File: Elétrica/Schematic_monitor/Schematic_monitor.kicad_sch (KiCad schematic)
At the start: 53 parts, among them J1 Conn_01x04, J2 USB_B_Micro, J3 Eletrode 1, J4 Eletrode 2, SW1 SW_Push, SW2 SW_SPDT, SW3 SW_SPDT, SW4 SW_SPDT, SW5 SW_SPDT, SW6 SW_SPDT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

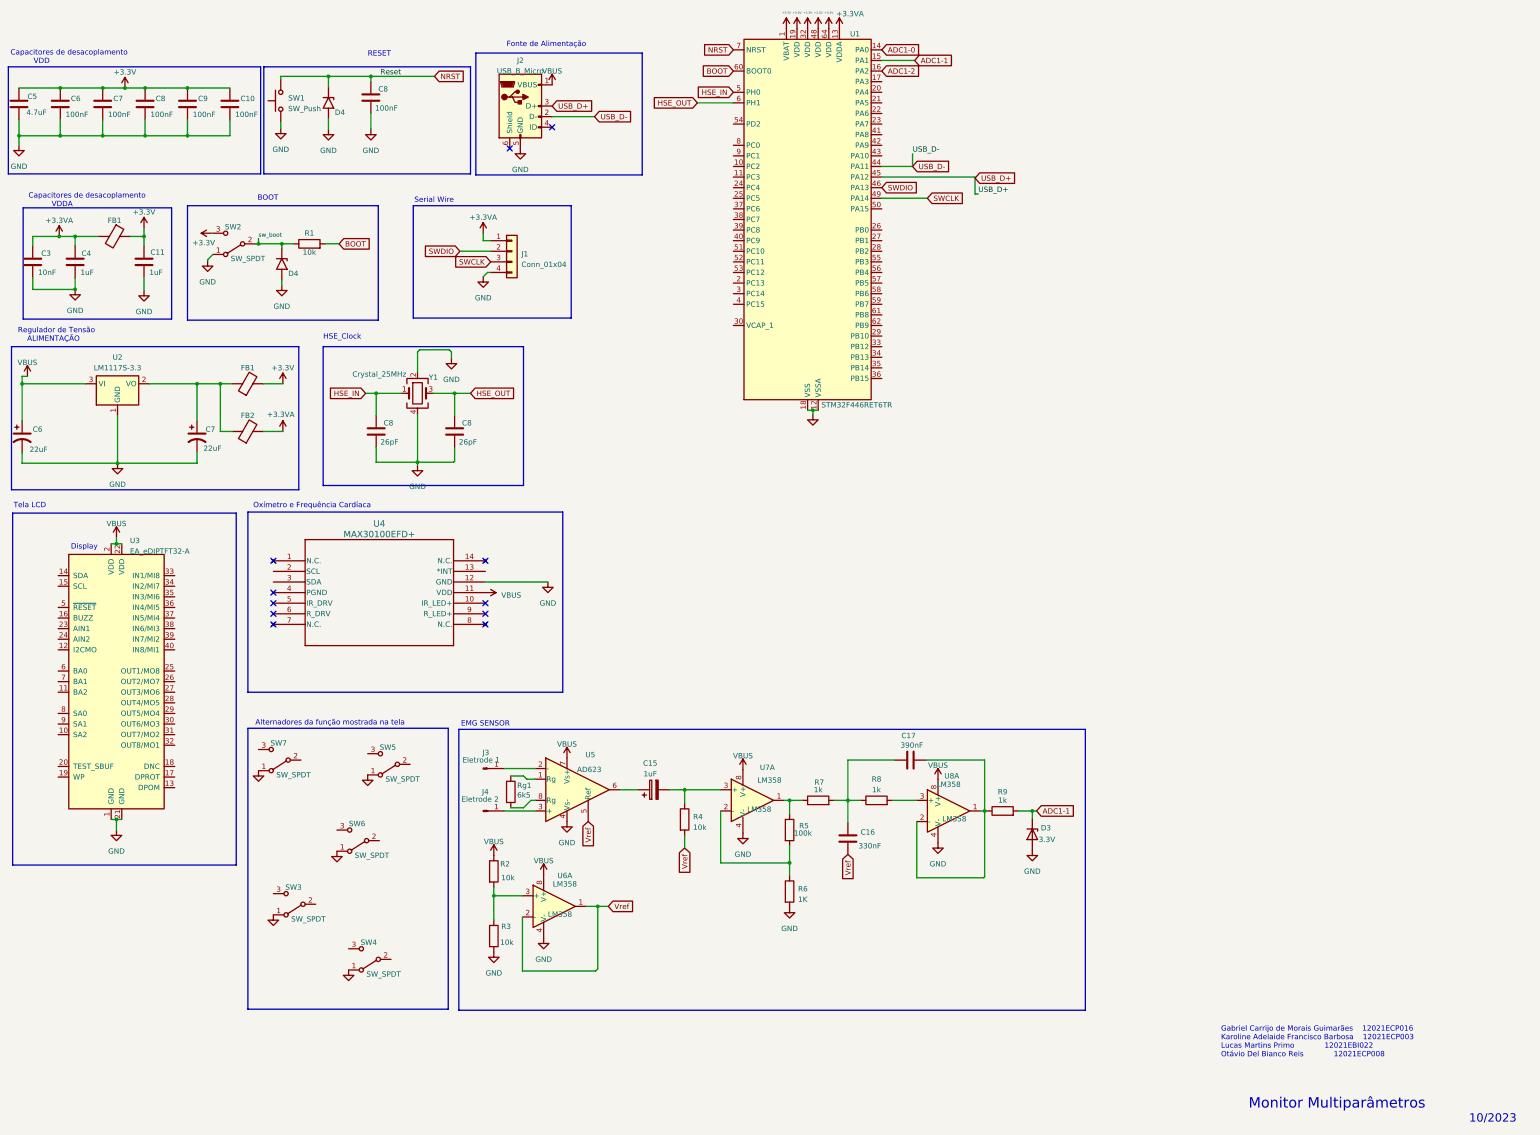
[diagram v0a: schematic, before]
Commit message: Correção Geral das pastas
Concertei diretório das pastas
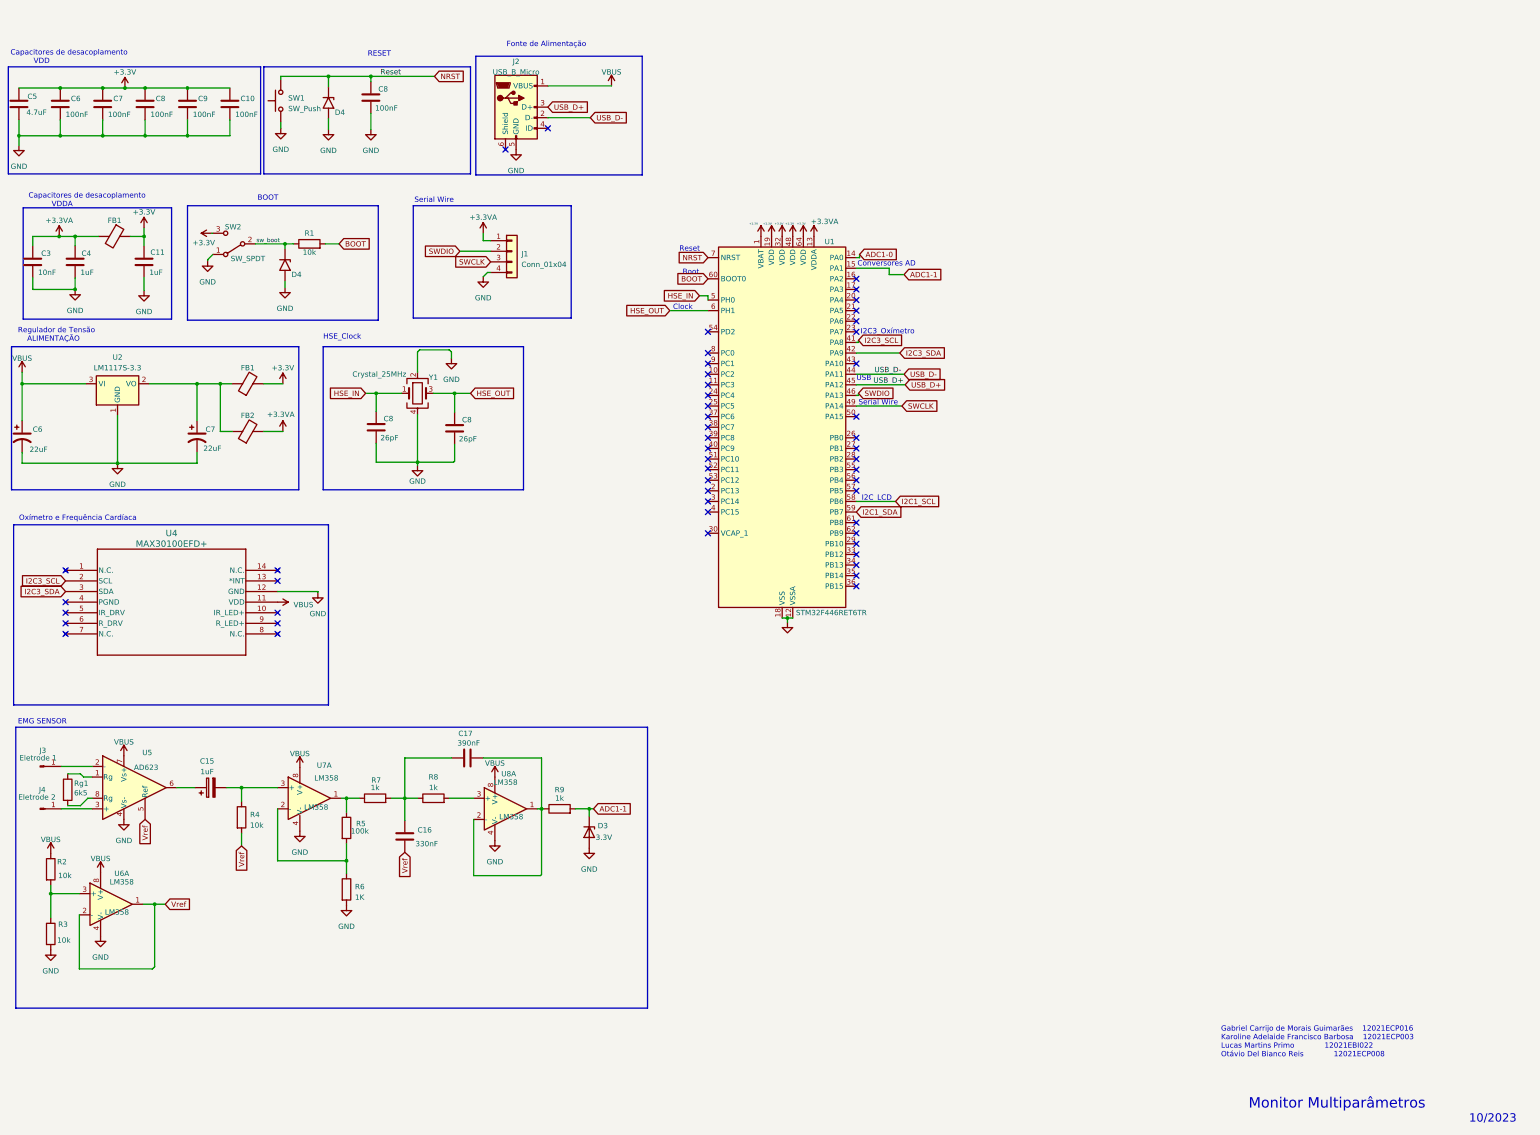
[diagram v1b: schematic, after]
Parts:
- removed SW3, SW4, SW5, SW6, SW7: SW_SPDT, Button_Switch_SMD:SW_DIP_SPSTx01_Slide_9.78x4.72mm_W8.61mm_P2.54mm, symbol Switch:SW_SPDT
- removed U3: EA_eDIPTFT32-A, Display:EA_eDIPTFT32-XXX, symbol Display_Graphic:EA_eDIPTFT32-A
- FB1: value FerriteBead -> New_Library:FerriteBead; footprint Inductor_SMD:L_0603_1608Metric -> Inductor_SMD:L_0603_1608Metric_Pad1.05x0.95mm_HandSolder
- FB2: footprint Inductor_SMD:L_0603_1608Metric -> Inductor_SMD:L_0603_1608Metric_Pad1.05x0.95mm_HandSolder
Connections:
- net I2C3_SCL: now reaches U4.2 (SCL)
- net I2C3_SCL: now also U1.41 (PA8)
- net I2C3_SDA: now reaches U4.3 (SDA)
- net I2C3_SDA: now also U1.42 (PA9)
- net I2C1_SCL: now reaches U1.58 (PB6)
- net I2C1_SDA: now reaches U1.59 (PB7)
- net ADC1-2: no longer names the net of U1.16 (PA2)
- no-connect marks 11 -> 51
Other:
- note added: "Boot"
- note added: "Clock"
- note added: "Conversores AD"
- note added: "I2C3_Oxímetro"
- note added: "I2C_LCD"
- note added: "Reset"
- note added: "USB"
- note removed: "Alternadores da função mostrada na tela"
- note removed: "Display"
- note removed: "Tela LCD"
- moved on the sheet: C15, C16, C17, C8, D3, D4, J2, J3, J4, R2, R3, R4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

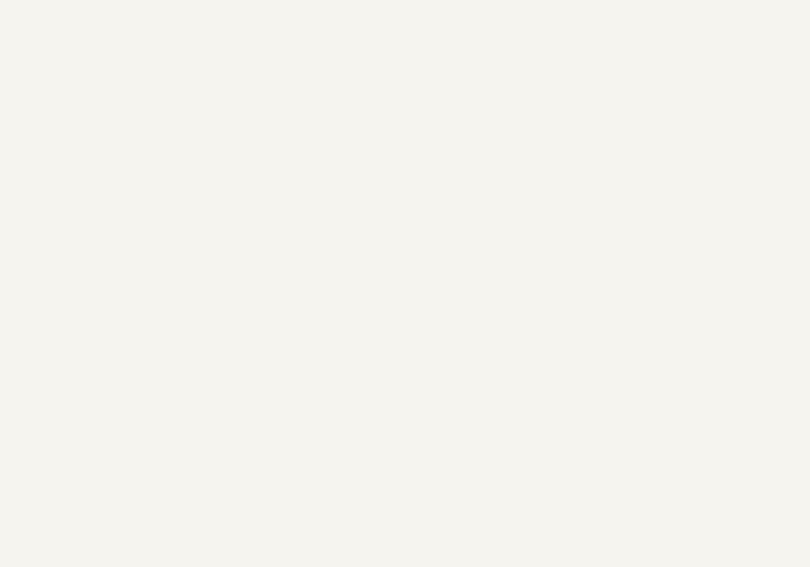
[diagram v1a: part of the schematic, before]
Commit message: Temp sensor
Adicionado sensor de temperatura
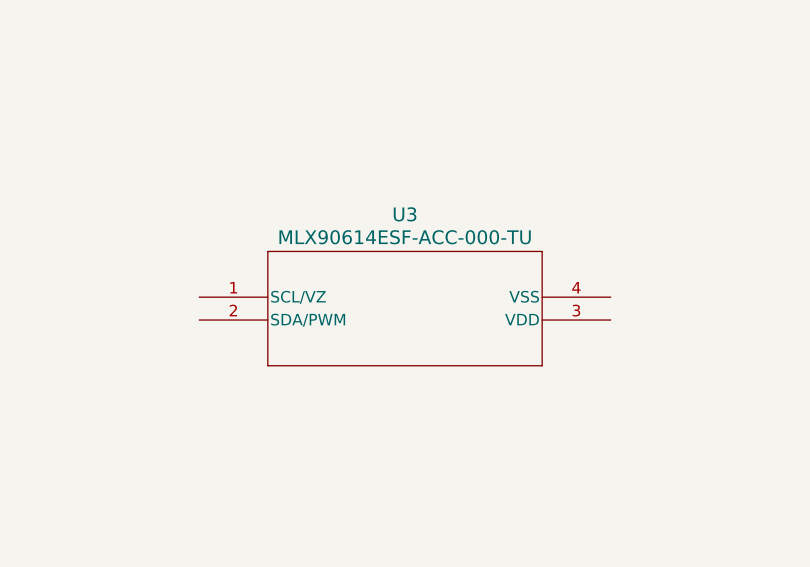
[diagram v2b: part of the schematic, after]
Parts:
- added U3: MLX90614ESF-ACC-000-TU, MLX90614xCC_MEL, symbol Temp_sensor:MLX90614ESF-ACC-000-TU
- C15: footprint Capacitor_SMD:C_Elec_3x5.4 -> Capacitor_SMD:C_0603_1608Metric_Pad1.08x0.95mm_HandSolder
- D3: footprint Diode_SMD:D_PowerDI-5 -> Diode_SMD:D_0603_1608Metric
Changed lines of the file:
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@@
       (effects (font (size 1.27 1.27)) (justify left))
     )
-    (property "Footprint" "Diode_SMD:D_PowerDI-5" (at 152.146 211.328 0)
+    (property "Footprint" "Diode_SMD:D_0603_1608Metric" (at 152.146 211.328 0)
       (effects (font (size 1.27 1.27)) hide)
     )
@@
       (effects (font (size 1.27 1.27)))
     )
-    (property "Footprint" "Capacitor_SMD:C_Elec_3x5.4" (at 65.278 199.6948 0)
+    (property "Footprint" "Capacitor_SMD:C_0603_1608Metric_Pad1.08x0.95mm_HandSolder" (at 65.278 199.6948 0)
       (effects (font (size 1.27 1.27)) hide)
     )
@@
         )
       )
+    )
+  )
+  (symbol (lib_id "Temp_sensor:MLX90614ESF-ACC-000-TU") (at 276.606 72.644 0) (unit 1)
+    (in_bom yes) (on_board yes) (dnp no) (fields_autoplaced)
+    (property "Reference" "U3" (at 299.466 63.5 0)
+      (effects (font (size 1.524 1.524)))
+    )
+    (property "Value" "MLX90614ESF-ACC-000-TU" (at 299.466 66.04 0)
+      (effects (font (size 1.524 1.524)))
+    )
+    (property "Footprint" "MLX90614xCC_MEL" (at 276.606 72.644 0)
+      (effects (font (size 1.27 1.27) italic) hide)
+    )
+    (property "Datasheet" "MLX90614ESF-ACC-000-TU" (at 276.606 72.644 0)
+      (effects (font (size 1.27 1.27) italic) hide)
+    )
+    (pin "1")
+    (pin "2")
+    (pin "3")
+    (pin "4")
+    (instances
+      (project "Schematic_monitor"
+        (path "/e9cd3b8d-6ac1-4cca-9ad1-0be06fd7b6c7"
+          (reference "U3") (unit 1)
+        )
+      )

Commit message: sensor de temperatura
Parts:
- added C18: 0.1uF, Capacitor_SMD:C_0603_1608Metric, symbol Device:C
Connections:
- net GND: now also U3.3 (VDD), U3.4 (VSS), C18.2
- net I2C1_SDA: now also U1.53 (PC12)
- net I2C3_SCL: now also U3.1 (SCL/VZ)
- net I2C3_SDA: now also U3.2 (SDA/PWM)
- net VBUS: now also C18.1
- no-connect marks 51 -> 49
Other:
- moved on the sheet: U3
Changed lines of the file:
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@@
   (junction (at 101.092 106.172) (diameter 0) (color 0 0 0 0)
+  )
+  (junction (at 153.924 154.94) (diameter 0) (color 0 0 0 0)
   )
   (junction (at 45.466 68.58) (diameter 0) (color 0 0 0 0)
@@
   (no_connect (at 216.154 144.78))
   (no_connect (at 216.154 78.74))
-  (no_connect (at 180.594 127))
   (no_connect (at 180.594 132.08))
   (no_connect (at 216.154 119.38))
@@
   (no_connect (at 77.47 161.29))
   (no_connect (at 77.47 158.75))
-  (no_connect (at 216.154 142.24))
   (no_connect (at 26.67 161.29))
   (wire (pts (xy 119.888 118.364) (xy 119.888 122.428))
@@
     (stroke (width 0) (type default))
   )
+  (wire (pts (xy 164.592 154.686) (xy 164.592 154.94))
+    (stroke (width 0) (type default))
+  )
   (wire (pts (xy 93.98 218.186) (xy 93.98 221.234))
     (stroke (width 0) (type default))
@@
     (stroke (width 0) (type default))
   )
+  (wire (pts (xy 164.592 154.94) (xy 161.544 154.94))
+    (stroke (width 0) (type default))
+  )
   (wire (pts (xy 216.916 72.898) (xy 216.916 73.66))
     (stroke (width 0) (type default))
@@
     (stroke (width 0) (type default))
   )
+  (wire (pts (xy 164.846 154.686) (xy 164.592 154.686))
+    (stroke (width 0) (type default))
+  )
   (wire (pts (xy 93.98 203.2) (xy 93.98 206.502))
     (stroke (width 0) (type default))
@@
     (stroke (width 0) (type default))
   )
+  (wire (pts (xy 152.4 154.94) (xy 153.924 154.94))
+    (stroke (width 0) (type default))
+  )
   (wire (pts (xy 45.72 40.64) (xy 45.72 44.45))
     (stroke (width 0) (type default))
@@
     (stroke (width 0) (type default))
   )
+  (wire (pts (xy 153.924 149.352) (xy 153.924 154.94))
+    (stroke (width 0) (type default))
+  )
   (wire (pts (xy 152.146 205.74) (xy 152.146 207.518))
     (stroke (width 0) (type default))
@@
     (stroke (width 0) (type default))
   )
+  (wire (pts (xy 152.4 157.48) (xy 153.924 157.48))
+    (stroke (width 0) (type default))
+  )
   (wire (pts (xy 68.834 200.66) (xy 77.47 200.66))
     (stroke (width 0) (type default))
@@
   )
   (wire (pts (xy 98.552 106.172) (xy 101.092 106.172))
+    (stroke (width 0) (type default))
+  )
+  (wire (pts (xy 153.924 157.48) (xy 153.924 154.94))
     (stroke (width 0) (type default))
   )
@@
     )
   )
+  (global_label "I2C1_SDA" (shape input) (at 180.594 127 180) (fields_autoplaced)
+    (effects (font (size 1.27 1.27)) (justify right))
+    (property "Intersheetrefs" "${INTERSHEET_REFS}" (at 168.7793 127 0)
+      (effects (font (size 1.27 1.27)) (justify right) hide)
+    )
+  )
+  (global_label "I2C3_SCL" (shape input) (at 106.68 154.94 180) (fields_autoplaced)
+    (effects (font (size 1.27 1.27)) (justify right))
+    (property "Intersheetrefs" "${INTERSHEET_REFS}" (at 94.9258 154.94 0)
+      (effects (font (size 1.27 1.27)) (justify right) hide)
+    )
+  )
   (global_label "I2C3_SCL" (shape input) (at 216.662 93.472 0) (fields_autoplaced)
     (effects (font (size 1.27 1.27)) (justify left))
@@
     )
   )
+  (global_label "I2C1_SCL" (shape input) (at 215.9 142.24 0) (fields_autoplaced)
+    (effects (font (size 1.27 1.27)) (justify left))
+    (property "Intersheetrefs" "${INTERSHEET_REFS}" (at 227.6542 142.24 0)
+      (effects (font (size 1.27 1.27)) (justify left) hide)
+    )
+  )
   (global_label "NRST" (shape input) (at 115.062 30.226 0) (fields_autoplaced)
     (effects (font (size 1.27 1.27)) (justify left))
@@
     )
   )
+  (global_label "I2C3_SDA" (shape input) (at 106.68 157.48 180) (fields_autoplaced)
+    (effects (font (size 1.27 1.27)) (justify right))
+    (property "Intersheetrefs" "${INTERSHEET_REFS}" (at 94.8653 157.48 0)
+      (effects (font (size 1.27 1.27)) (justify right) hide)
+    )
+  )
   (symbol (lib_id "power:VBUS") (at 157.48 32.512 0) (unit 1)
     (in_bom yes) (on_board yes) (dnp no) (fields_autoplaced)
@@
     )
   )
+  (symbol (lib_id "power:VBUS") (at 164.846 154.686 270) (unit 1)
+    (in_bom yes) (on_board yes) (dnp no) (fields_autoplaced)
+    (property "Reference" "#PWR030" (at 161.036 154.686 0)
+      (effects (font (size 1.27 1.27)) hide)
+    )
+    (property "Value" "VBUS" (at 168.656 155.321 90)
+      (effects (font (size 1.27 1.27)) (justify left))
+    )
+    (property "Footprint" "" (at 164.846 154.686 0)
+      (effects (font (size 1.27 1.27)) hide)
+    )
+    (property "Datasheet" "" (at 164.846 154.686 0)
+      (effects (font (size 1.27 1.27)) hide)
+    )
+    (pin "1")
+    (instances
+      (project "Schematic_monitor"
+        (path "/e9cd3b8d-6ac1-4cca-9ad1-0be06fd7b6c7"
+          (reference "#PWR030") (unit 1)
+        )
+      )
+    )
+  )
   (symbol (lib_id "Connector:Conn_01x01_Pin") (at 20.574 195.58 0) (unit 1)
     (in_bom yes) (on_board yes) (dnp no)
@@
         (path "/e9cd3b8d-6ac1-4cca-9ad1-0be06fd7b6c7"
           (reference "#PWR035") (unit 1)
+        )
+      )
+    )
+  )
+  (symbol (lib_id "Device:C") (at 157.734 154.94 270) (unit 1)
+    (in_bom yes) (on_board yes) (dnp no) (fields_autoplaced)
+    (property "Reference" "C18" (at 157.734 147.32 90)
+      (effects (font (size 1.27 1.27)))
+    )
+    (property "Value" "0.1uF" (at 157.734 149.86 90)
+      (effects (font (size 1.27 1.27)))
+    )
+    (property "Footprint" "Capacitor_SMD:C_0603_1608Metric" (at 153.924 155.9052 0)
+      (effects (font (size 1.27 1.27)) hide)
+    )
+    (property "Datasheet" "~" (at 157.734 154.94 0)
+      (effects (font (size 1.27 1.27)) hide)
+    )
+    (pin "1")
+    (pin "2")
+    (instances
+      (project "Schematic_monitor"
+        (path "/e9cd3b8d-6ac1-4cca-9ad1-0be06fd7b6c7"
+          (reference "C18") (unit 1)
         )
       )
@@
     )
   )
+  (symbol (lib_id "power:GND") (at 153.924 149.352 180) (unit 1)
+    (in_bom yes) (on_board yes) (dnp no) (fields_autoplaced)
+    (property "Reference" "#PWR027" (at 153.924 143.002 0)
+      (effects (font (size 1.27 1.27)) hide)
+    )
+    (property "Value" "GND" (at 153.924 144.272 0)
+      (effects (font (size 1.27 1.27)))
+    )
+    (property "Footprint" "" (at 153.924 149.352 0)
+      (effects (font (size 1.27 1.27)) hide)
+    )
+    (property "Datasheet" "" (at 153.924 149.352 0)
+      (effects (font (size 1.27 1.27)) hide)
+    )
+    (pin "1")
+    (instances
+      (project "ProjetoSEMB_Gabriel_Rafael"
+        (path "/71af4175-d518-4051-8306-cd60f2e5793a"
+          (reference "#PWR027") (unit 1)
+        )
+      )
+      (project "Schematic_monitor"
+        (path "/e9cd3b8d-6ac1-4cca-9ad1-0be06fd7b6c7"
+          (reference "#PWR031") (unit 1)
+        )
+      )
+    )
+  )
   (symbol (lib_id "Device:C") (at 107.95 212.344 0) (unit 1)
     (in_bom yes) (on_board yes) (dnp no)
@@
     )
   )
-  (symbol (lib_id "Temp_sensor:MLX90614ESF-ACC-000-TU") (at 276.606 72.644 0) (unit 1)
-    (in_bom yes) (on_board yes) (dnp no) (fields_autoplaced)
-    (property "Reference" "U3" (at 299.466 63.5 0)
+  (symbol (lib_id "Temp_sensor:MLX90614ESF-ACC-000-TU") (at 106.68 154.94 0) (unit 1)
+    (in_bom yes) (on_board yes) (dnp no) (fields_autoplaced)
+    (property "Reference" "U3" (at 129.54 145.796 0)
       (effects (font (size 1.524 1.524)))
     )
-    (property "Value" "MLX90614ESF-ACC-000-TU" (at 299.466 66.04 0)
+    (property "Value" "MLX90614ESF-ACC-000-TU" (at 129.54 148.336 0)
       (effects (font (size 1.524 1.524)))
     )
-    (property "Footprint" "MLX90614xCC_MEL" (at 276.606 72.644 0)
+    (property "Footprint" "MLX90614xCC_MEL" (at 106.68 154.94 0)
       (effects (font (size 1.27 1.27) italic) hide)
     )
-    (property "Datasheet" "MLX90614ESF-ACC-000-TU" (at 276.606 72.644 0)
+    (property "Datasheet" "MLX90614ESF-ACC-000-TU" (at 106.68 154.94 0)
       (effects (font (size 1.27 1.27) italic) hide)
     )
